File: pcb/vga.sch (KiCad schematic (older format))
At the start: 23 parts

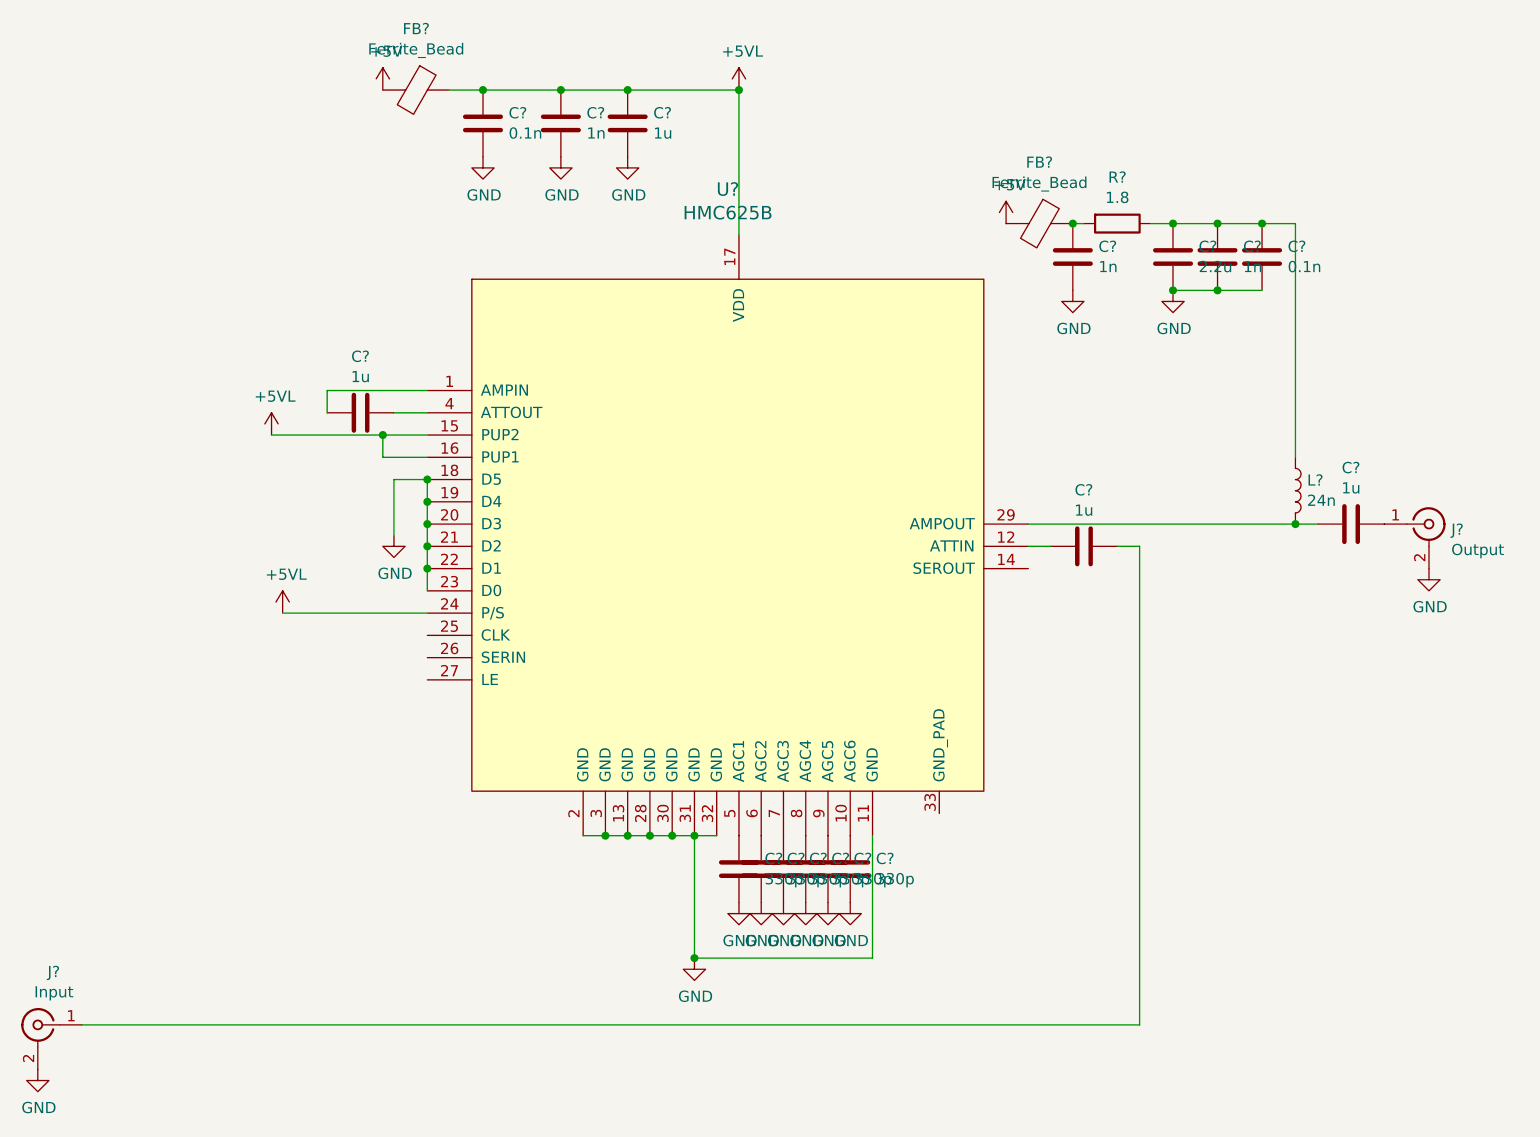
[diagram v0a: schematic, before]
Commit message: Add STM32L010C6 mcu to pcb, allocate pins
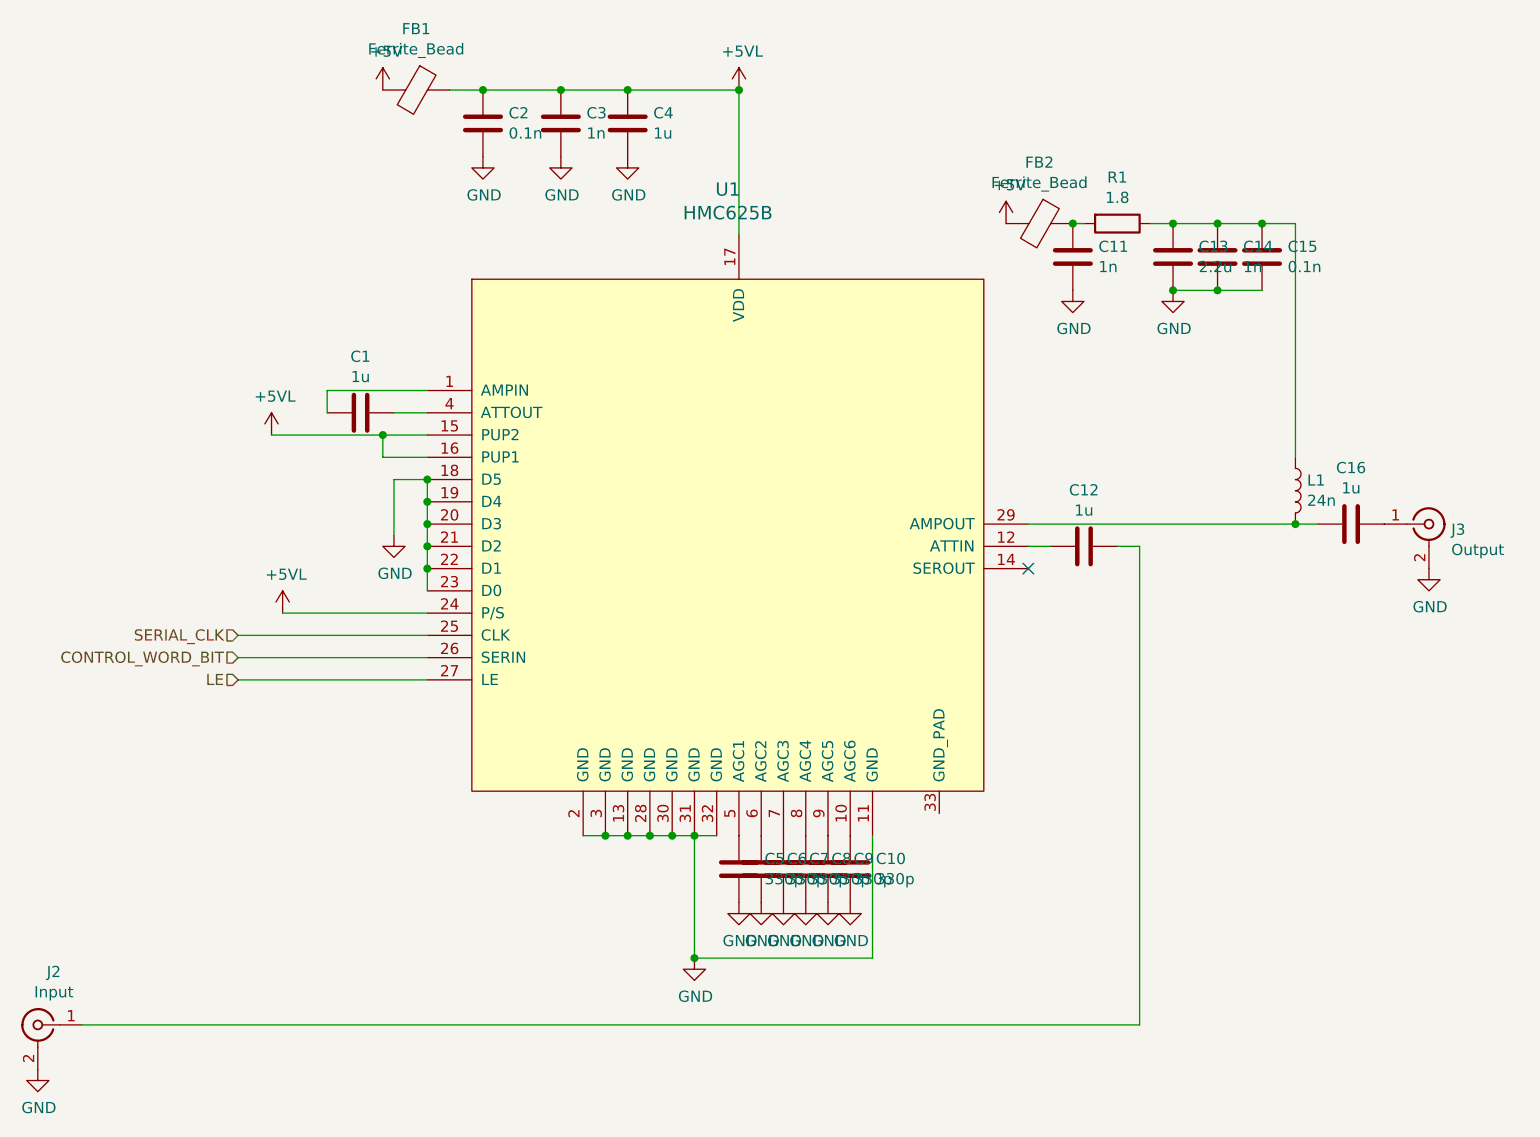
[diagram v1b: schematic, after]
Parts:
- C1, C10, C11, C12, C13, C14, C15, C16, C2, C3, C4, C5, C6, C7, C8, C9: renamed from C?; footprint (none) -> Capacitor_SMD:C_0603_1608Metric
- L1: renamed from L?; footprint (none) -> Inductor_SMD:L_0603_1608Metric
- R1: renamed from R?; footprint (none) -> Resistor_SMD:R_0603_1608Metric
- U1: renamed from U?; footprint (none) -> Package_DFN_QFN:QFN-32-1EP_5x5mm_P0.5mm_EP3.45x3.45mm_ThermalVias
- gave numbers to parts that had none: 4
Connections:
- net SERIAL_CLK: now reaches U1.25 (CLK)
- net CONTROL_WORD_BIT: now reaches U1.26 (SERIN)
- net LE: now reaches U1.27 (LE)
- no-connect marks 0 -> 1

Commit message: PCB updates
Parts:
- FB1, FB2: value Ferrite_Bead -> GZ2012D601TF
- J2, J3: footprint (none) -> parts:SMA_Samtec_SMA-J-P-X-ST-EM1_EdgeMount_withSTEP
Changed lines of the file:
@@
 $Descr A4 11693 8268
 encoding utf-8
-Sheet 2 3
+Sheet 2 4
 Title ""
 Date ""
@@
 F 0 "J3" H 9500 3525 50  0000 L CNN
 F 1 "Output" H 9500 3434 50  0000 L CNN
-F 2 "" H 9400 3550 50  0001 C CNN
+F 2 "parts:SMA_Samtec_SMA-J-P-X-ST-EM1_EdgeMount_withSTEP" H 9400 3550 50  0001 C CNN
 F 3 " ~" H 9400 3550 50  0001 C CNN
 	1    9400 3550
@@
 P 7650 2200
 F 0 "FB2" V 7376 2200 50  0000 C CNN
-F 1 "Ferrite_Bead" V 7467 2200 50  0000 C CNN
+F 1 "GZ2012D601TF" V 7467 2200 50  0000 C CNN
 F 2 "" V 7580 2200 50  0001 C CNN
 F 3 "~" H 7650 2200 50  0001 C CNN
@@
 F 0 "J2" H 3078 6038 50  0000 C CNN
 F 1 "Input" H 3078 5947 50  0000 C CNN
-F 2 "" H 3150 5800 50  0001 C CNN
+F 2 "parts:SMA_Samtec_SMA-J-P-X-ST-EM1_EdgeMount_withSTEP" H 3150 5800 50  0001 C CNN
 F 3 " ~" H 3150 5800 50  0001 C CNN
 	1    3150 5800
@@
 P 4850 1600
 F 0 "FB1" V 4576 1600 50  0000 C CNN
-F 1 "Ferrite_Bead" V 4667 1600 50  0000 C CNN
+F 1 "GZ2012D601TF" V 4667 1600 50  0000 C CNN
 F 2 "" V 4780 1600 50  0001 C CNN
 F 3 "~" H 4850 1600 50  0001 C CNN

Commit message: layout check in
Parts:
- C1, C16: value 1u -> 0.1u; footprint Capacitor_SMD:C_0603_1608Metric -> Capacitor_SMD:C_0402_1005Metric
- C10, C11, C12, C13, C14, C15, C2, C3, C4, C5, C6, C7, C8, C9: footprint Capacitor_SMD:C_0603_1608Metric -> Capacitor_SMD:C_0402_1005Metric
- FB1, FB2: footprint (none) -> Inductor_SMD:L_0603_1608Metric
- L1: value 24n -> 3.5u; footprint Inductor_SMD:L_0603_1608Metric -> 4310LC:4310LC
- R1: footprint Resistor_SMD:R_0603_1608Metric -> Resistor_SMD:R_0402_1005Metric
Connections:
- net GND: now also U1.33 (GND_PAD)
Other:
- moved on the sheet: C11, C13, C14, C15, FB2, L1, R1
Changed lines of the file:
@@
 F 0 "C2" H 5265 1796 50  0000 L CNN
 F 1 "0.1n" H 5265 1705 50  0000 L CNN
-F 2 "Capacitor_SMD:C_0603_1608Metric" H 5188 1600 50  0001 C CNN
+F 2 "Capacitor_SMD:C_0402_1005Metric" H 5188 1600 50  0001 C CNN
 F 3 "~" H 5150 1750 50  0001 C CNN
 	1    5150 1750
@@
 F 0 "C3" H 5615 1796 50  0000 L CNN
 F 1 "1n" H 5615 1705 50  0000 L CNN
-F 2 "Capacitor_SMD:C_0603_1608Metric" H 5538 1600 50  0001 C CNN
+F 2 "Capacitor_SMD:C_0402_1005Metric" H 5538 1600 50  0001 C CNN
 F 3 "~" H 5500 1750 50  0001 C CNN
 	1    5500 1750
@@
 F 0 "C4" H 5915 1796 50  0000 L CNN
 F 1 "1u" H 5915 1705 50  0000 L CNN
-F 2 "Capacitor_SMD:C_0603_1608Metric" H 5838 1600 50  0001 C CNN
+F 2 "Capacitor_SMD:C_0402_1005Metric" H 5838 1600 50  0001 C CNN
 F 3 "~" H 5800 1750 50  0001 C CNN
 	1    5800 1750
@@
 F 0 "C5" H 6415 5146 50  0000 L CNN
 F 1 "330p" H 6415 5055 50  0000 L CNN
-F 2 "Capacitor_SMD:C_0603_1608Metric" H 6338 4950 50  0001 C CNN
+F 2 "Capacitor_SMD:C_0402_1005Metric" H 6338 4950 50  0001 C CNN
 F 3 "~" H 6300 5100 50  0001 C CNN
 	1    6300 5100
@@
 F 0 "C6" H 6515 5146 50  0000 L CNN
 F 1 "330p" H 6515 5055 50  0000 L CNN
-F 2 "Capacitor_SMD:C_0603_1608Metric" H 6438 4950 50  0001 C CNN
+F 2 "Capacitor_SMD:C_0402_1005Metric" H 6438 4950 50  0001 C CNN
 F 3 "~" H 6400 5100 50  0001 C CNN
 	1    6400 5100
@@
 F 0 "C7" H 6615 5146 50  0000 L CNN
 F 1 "330p" H 6615 5055 50  0000 L CNN
-F 2 "Capacitor_SMD:C_0603_1608Metric" H 6538 4950 50  0001 C CNN
+F 2 "Capacitor_SMD:C_0402_1005Metric" H 6538 4950 50  0001 C CNN
 F 3 "~" H 6500 5100 50  0001 C CNN
 	1    6500 5100
@@
 F 0 "C8" H 6715 5146 50  0000 L CNN
 F 1 "330p" H 6715 5055 50  0000 L CNN
-F 2 "Capacitor_SMD:C_0603_1608Metric" H 6638 4950 50  0001 C CNN
+F 2 "Capacitor_SMD:C_0402_1005Metric" H 6638 4950 50  0001 C CNN
 F 3 "~" H 6600 5100 50  0001 C CNN
 	1    6600 5100
@@
 F 0 "C9" H 6815 5146 50  0000 L CNN
 F 1 "330p" H 6815 5055 50  0000 L CNN
-F 2 "Capacitor_SMD:C_0603_1608Metric" H 6738 4950 50  0001 C CNN
+F 2 "Capacitor_SMD:C_0402_1005Metric" H 6738 4950 50  0001 C CNN
 F 3 "~" H 6700 5100 50  0001 C CNN
 	1    6700 5100
@@
 F 0 "C10" H 6915 5146 50  0000 L CNN
 F 1 "330p" H 6915 5055 50  0000 L CNN
-F 2 "Capacitor_SMD:C_0603_1608Metric" H 6838 4950 50  0001 C CNN
+F 2 "Capacitor_SMD:C_0402_1005Metric" H 6838 4950 50  0001 C CNN
 F 3 "~" H 6800 5100 50  0001 C CNN
 	1    6800 5100
@@
 P 4600 3050
 F 0 "C1" V 4348 3050 50  0000 C CNN
-F 1 "1u" V 4439 3050 50  0000 C CNN
-F 2 "Capacitor_SMD:C_0603_1608Metric" H 4638 2900 50  0001 C CNN
+F 1 "0.1u" V 4439 3050 50  0000 C CNN
+F 2 "Capacitor_SMD:C_0402_1005Metric" H 4638 2900 50  0001 C CNN
 F 3 "~" H 4600 3050 50  0001 C CNN
 	1    4600 3050
@@
 Wire Wire Line
 	4450 2950 4900 2950
-Wire Wire Line
-	7600 3550 8800 3550
 $Comp
 L Device:C C16
@@
 P 9050 3550
 F 0 "C16" V 8798 3550 50  0000 C CNN
-F 1 "1u" V 8889 3550 50  0000 C CNN
-F 2 "Capacitor_SMD:C_0603_1608Metric" H 9088 3400 50  0001 C CNN
+F 1 "0.1u" V 8889 3550 50  0000 C CNN
+F 2 "Capacitor_SMD:C_0402_1005Metric" H 9088 3400 50  0001 C CNN
 F 3 "~" H 9050 3550 50  0001 C CNN
 	1    9050 3550
@@
 $EndComp
 $Comp
-L Device:L L1
-U 1 1 613E8F30
-P 8800 3400
-F 0 "L1" H 8852 3446 50  0000 L CNN
-F 1 "24n" H 8852 3355 50  0000 L CNN
-F 2 "Inductor_SMD:L_0603_1608Metric" H 8800 3400 50  0001 C CNN
-F 3 "~" H 8800 3400 50  0001 C CNN
-	1    8800 3400
-	1    0    0    -1
-$EndComp
-Connection ~ 8800 3550
-Wire Wire Line
-	8800 3550 8900 3550
-$Comp
 L Device:C C13
 U 1 1 613E8F38
-P 8250 2350
-F 0 "C13" H 8365 2396 50  0000 L CNN
-F 1 "2.2u" H 8365 2305 50  0000 L CNN
-F 2 "Capacitor_SMD:C_0603_1608Metric" H 8288 2200 50  0001 C CNN
-F 3 "~" H 8250 2350 50  0001 C CNN
-	1    8250 2350
+P 8200 1850
+F 0 "C13" H 8315 1896 50  0000 L CNN
+F 1 "2.2u" H 8315 1805 50  0000 L CNN
+F 2 "Capacitor_SMD:C_0402_1005Metric" H 8238 1700 50  0001 C CNN
+F 3 "~" H 8200 1850 50  0001 C CNN
+	1    8200 1850
 	1    0    0    -1
 $EndComp
@@
 L Device:C C14
 U 1 1 613E8F3E
-P 8450 2350
-F 0 "C14" H 8565 2396 50  0000 L CNN
-F 1 "1n" H 8565 2305 50  0000 L CNN
-F 2 "Capacitor_SMD:C_0603_1608Metric" H 8488 2200 50  0001 C CNN
-F 3 "~" H 8450 2350 50  0001 C CNN
-	1    8450 2350
+P 8400 1850
+F 0 "C14" H 8515 1896 50  0000 L CNN
+F 1 "1n" H 8515 1805 50  0000 L CNN
+F 2 "Capacitor_SMD:C_0402_1005Metric" H 8438 1700 50  0001 C CNN
+F 3 "~" H 8400 1850 50  0001 C CNN
+	1    8400 1850
 	1    0    0    -1
 $EndComp
@@
 L Device:C C15
 U 1 1 613E8F44
-P 8650 2350
-F 0 "C15" H 8765 2396 50  0000 L CNN
-F 1 "0.1n" H 8765 2305 50  0000 L CNN
-F 2 "Capacitor_SMD:C_0603_1608Metric" H 8688 2200 50  0001 C CNN
-F 3 "~" H 8650 2350 50  0001 C CNN
-	1    8650 2350
+P 8600 1850
+F 0 "C15" H 8715 1896 50  0000 L CNN
+F 1 "0.1n" H 8715 1805 50  0000 L CNN
+F 2 "Capacitor_SMD:C_0402_1005Metric" H 8638 1700 50  0001 C CNN
+F 3 "~" H 8600 1850 50  0001 C CNN
+	1    8600 1850
 	1    0    0    -1
 $EndComp
@@
 L power:GND #PWR019
 U 1 1 613E8F4A
-P 8250 2500
-F 0 "#PWR019" H 8250 2250 50  0001 C CNN
-F 1 "GND" H 8255 2327 50  0000 C CNN
-F 2 "" H 8250 2500 50  0001 C CNN
-F 3 "" H 8250 2500 50  0001 C CNN
-	1    8250 2500
-	1    0    0    -1
-$EndComp
-Wire Wire Line
-	8650 2500 8450 2500
-Connection ~ 8250 2500
-Connection ~ 8450 2500
-Wire Wire Line
-	8450 2500 8250 2500
-Wire Wire Line
-	8250 2200 8450 2200
-Connection ~ 8450 2200
-Wire Wire Line
-	8450 2200 8650 2200
-Wire Wire Line
-	8800 3250 8800 2200
-Connection ~ 8650 2200
+P 8200 2000
+F 0 "#PWR019" H 8200 1750 50  0001 C CNN
+F 1 "GND" H 8205 1827 50  0000 C CNN
+F 2 "" H 8200 2000 50  0001 C CNN
+F 3 "" H 8200 2000 50  0001 C CNN
+	1    8200 2000
+	1    0    0    -1
+$EndComp
+Wire Wire Line
+	8600 2000 8400 2000
+Connection ~ 8200 2000
+Connection ~ 8400 2000
+Wire Wire Line
+	8400 2000 8200 2000
+Wire Wire Line
+	8200 1700 8400 1700
+Connection ~ 8400 1700
+Wire Wire Line
+	8400 1700 8600 1700
+Connection ~ 8600 1700
 $Comp
 L Device:R R1
 U 1 1 613E8F59
-P 8000 2200
-F 0 "R1" V 7793 2200 50  0000 C CNN
-F 1 "1.8" V 7884 2200 50  0000 C CNN
-F 2 "Resistor_SMD:R_0603_1608Metric" V 7930 2200 50  0001 C CNN
-F 3 "~" H 8000 2200 50  0001 C CNN
-	1    8000 2200
+P 7950 1700
+F 0 "R1" V 7743 1700 50  0000 C CNN
+F 1 "1.8" V 7834 1700 50  0000 C CNN
+F 2 "Resistor_SMD:R_0402_1005Metric" V 7880 1700 50  0000 C CNN
+F 3 "~" H 7950 1700 50  0001 C CNN
+	1    7950 1700
 	0    1    1    0
 $EndComp
@@
 L power:+5V #PWR017
 U 1 1 613E8F5F
-P 7500 2200
-F 0 "#PWR017" H 7500 2050 50  0001 C CNN
-F 1 "+5V" H 7515 2373 50  0000 C CNN
-F 2 "" H 7500 2200 50  0001 C CNN
-F 3 "" H 7500 2200 50  0001 C CNN
-	1    7500 2200
+P 7450 1700
+F 0 "#PWR017" H 7450 1550 50  0001 C CNN
+F 1 "+5V" H 7465 1873 50  0000 C CNN
+F 2 "" H 7450 1700 50  0001 C CNN
+F 3 "" H 7450 1700 50  0001 C CNN
+	1    7450 1700
 	1    0    0    -1
 $EndComp
@@
 L Device:Ferrite_Bead FB2
 U 1 1 613E8F65
-P 7650 2200
-F 0 "FB2" V 7376 2200 50  0000 C CNN
-F 1 "GZ2012D601TF" V 7467 2200 50  0000 C CNN
-F 2 "" V 7580 2200 50  0001 C CNN
-F 3 "~" H 7650 2200 50  0001 C CNN
-	1    7650 2200
+P 7600 1700
+F 0 "FB2" V 7326 1700 50  0000 C CNN
+F 1 "GZ2012D601TF" V 7417 1700 50  0000 C CNN
+F 2 "Inductor_SMD:L_0603_1608Metric" V 7530 1700 50  0001 C CNN
+F 3 "~" H 7600 1700 50  0001 C CNN
+	1    7600 1700
 	0    1    1    0
 $EndComp
@@
 L Device:C C11
 U 1 1 613E8F6B
-P 7800 2350
-F 0 "C11" H 7915 2396 50  0000 L CNN
-F 1 "1n" H 7915 2305 50  0000 L CNN
-F 2 "Capacitor_SMD:C_0603_1608Metric" H 7838 2200 50  0001 C CNN
-F 3 "~" H 7800 2350 50  0001 C CNN
-	1    7800 2350
+P 7750 1850
+F 0 "C11" H 7865 1896 50  0000 L CNN
+F 1 "1n" H 7865 1805 50  0000 L CNN
+F 2 "Capacitor_SMD:C_0402_1005Metric" H 7788 1700 50  0001 C CNN
+F 3 "~" H 7750 1850 50  0001 C CNN
+	1    7750 1850
 	1    0    0    -1
 $EndComp
@@
 L power:GND #PWR018
 U 1 1 613E8F71
-P 7800 2500
-F 0 "#PWR018" H 7800 2250 50  0001 C CNN
-F 1 "GND" H 7805 2327 50  0000 C CNN
-F 2 "" H 7800 2500 50  0001 C CNN
-F 3 "" H 7800 2500 50  0001 C CNN
-	1    7800 2500
-	1    0    0    -1
-$EndComp
-Wire Wire Line
-	7850 2200 7800 2200
-Connection ~ 7800 2200
-Wire Wire Line
-	8150 2200 8250 2200
-Connection ~ 8250 2200
-Wire Wire Line
-	8800 2200 8650 2200
+P 7750 2000
+F 0 "#PWR018" H 7750 1750 50  0001 C CNN
+F 1 "GND" H 7755 1827 50  0000 C CNN
+F 2 "" H 7750 2000 50  0001 C CNN
+F 3 "" H 7750 2000 50  0001 C CNN
+	1    7750 2000
+	1    0    0    -1
+$EndComp
+Wire Wire Line
+	7800 1700 7750 1700
+Connection ~ 7750 1700
+Wire Wire Line
+	8100 1700 8200 1700
+Connection ~ 8200 1700
 $Comp
 L Connector:Conn_Coaxial J2
@@
 F 0 "C12" V 7598 3650 50  0000 C CNN
 F 1 "1u" V 7689 3650 50  0000 C CNN
-F 2 "Capacitor_SMD:C_0603_1608Metric" H 7888 3500 50  0001 C CNN
+F 2 "Capacitor_SMD:C_0402_1005Metric" H 7888 3500 50  0001 C CNN
 F 3 "~" H 7850 3650 50  0001 C CNN
 	1    7850 3650
@@
 F 0 "FB1" V 4576 1600 50  0000 C CNN
 F 1 "GZ2012D601TF" V 4667 1600 50  0000 C CNN
-F 2 "" V 4780 1600 50  0001 C CNN
+F 2 "Inductor_SMD:L_0603_1608Metric" V 4780 1600 50  0001 C CNN
 F 3 "~" H 4850 1600 50  0001 C CNN
 	1    4850 1600
@@
 	4900 4150 4050 4150
 NoConn ~ 7600 3750
+Connection ~ 8800 3550
+Wire Wire Line
+	8800 3550 8900 3550
+Wire Wire Line
+	7600 3550 8800 3550
+$Comp
+L Device:L L1
+U 1 1 613E8F30
+P 8800 3050
+F 0 "L1" H 8852 3096 50  0000 L CNN
+F 1 "3.5u" H 8852 3005 50  0000 L CNN
+F 2 "4310LC:4310LC" H 8800 3050 50  0001 C CNN
+F 3 "4310LC-352" H 8800 3050 50  0001 C CNN
+	1    8800 3050
+	1    0    0    -1
+$EndComp
+Wire Wire Line
+	8800 3200 8800 3550
+Wire Wire Line
+	8800 2900 8800 1700
+Wire Wire Line
+	8600 1700 8800 1700
+$Comp
+L power:GND #PWR0104
+U 1 1 6145F84C
+P 7200 4850
+F 0 "#PWR0104" H 7200 4600 50  0001 C CNN
+F 1 "GND" H 7205 4677 50  0000 C CNN
+F 2 "" H 7200 4850 50  0001 C CNN
+F 3 "" H 7200 4850 50  0001 C CNN
+	1    7200 4850
+	1    0    0    -1
+$EndComp
 $EndSCHEMATC

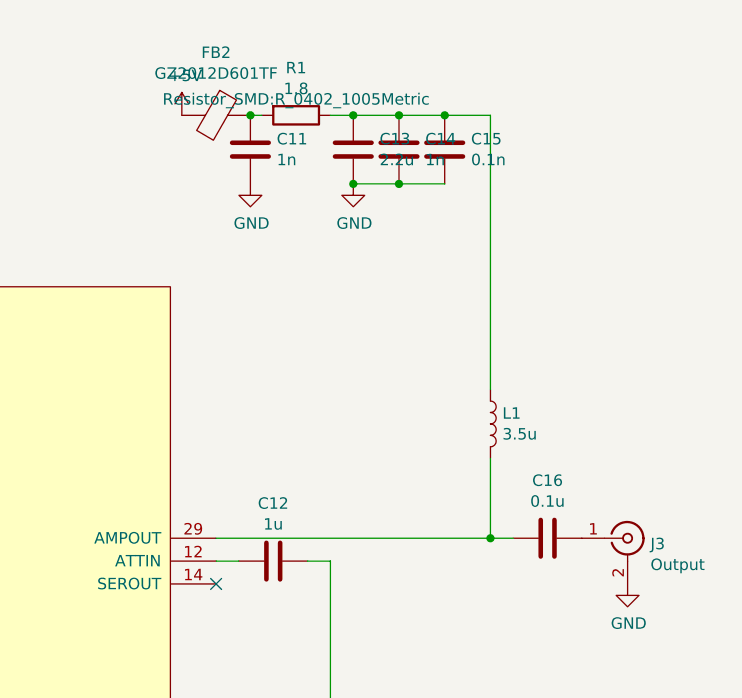
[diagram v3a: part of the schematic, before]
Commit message: Completed PCB layout
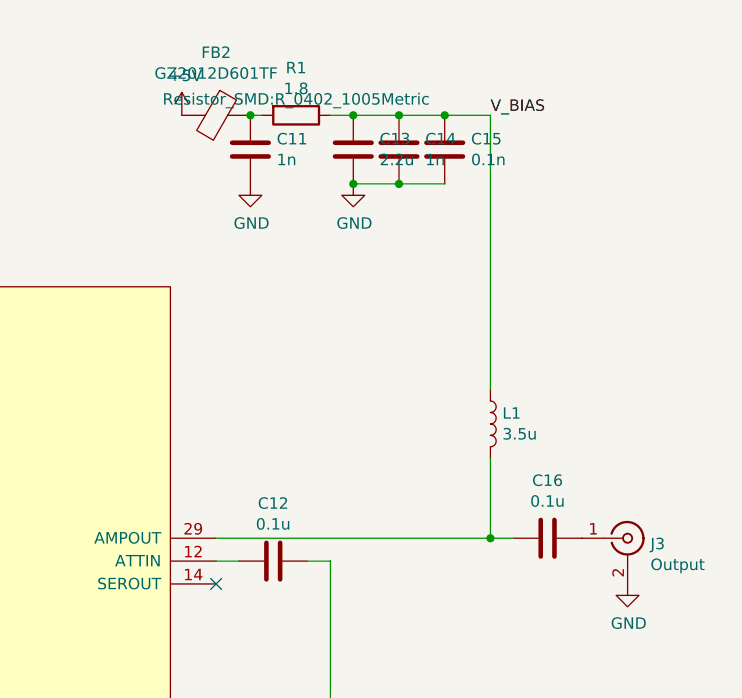
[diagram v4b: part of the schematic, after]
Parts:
- C12: value 1u -> 0.1u
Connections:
- net V_BIAS: now reaches C13.1, C14.1, C15.1, L1.1, R1.1
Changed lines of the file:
@@
 P 7850 3650
 F 0 "C12" V 7598 3650 50  0000 C CNN
-F 1 "1u" V 7689 3650 50  0000 C CNN
+F 1 "0.1u" V 7689 3650 50  0000 C CNN
 F 2 "Capacitor_SMD:C_0402_1005Metric" H 7888 3500 50  0001 C CNN
 F 3 "~" H 7850 3650 50  0001 C CNN
@@
 	1    0    0    -1
 $EndComp
+Text Label 8800 1700 0    50   ~ 0
+V_BIAS
 $EndSCHEMATC
